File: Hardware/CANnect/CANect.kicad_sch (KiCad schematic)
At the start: 15 parts, among them J1 USB_C_Receptacle_USB2.0_16P, J2 Micro_SD_Card, J3 Conn_01x02_Pin, U1 SN65HVD230, U2 ESP32-S3-WROOM-1, U3 USBLC6-2SC6, U4 AP2114H-3.3TRG1

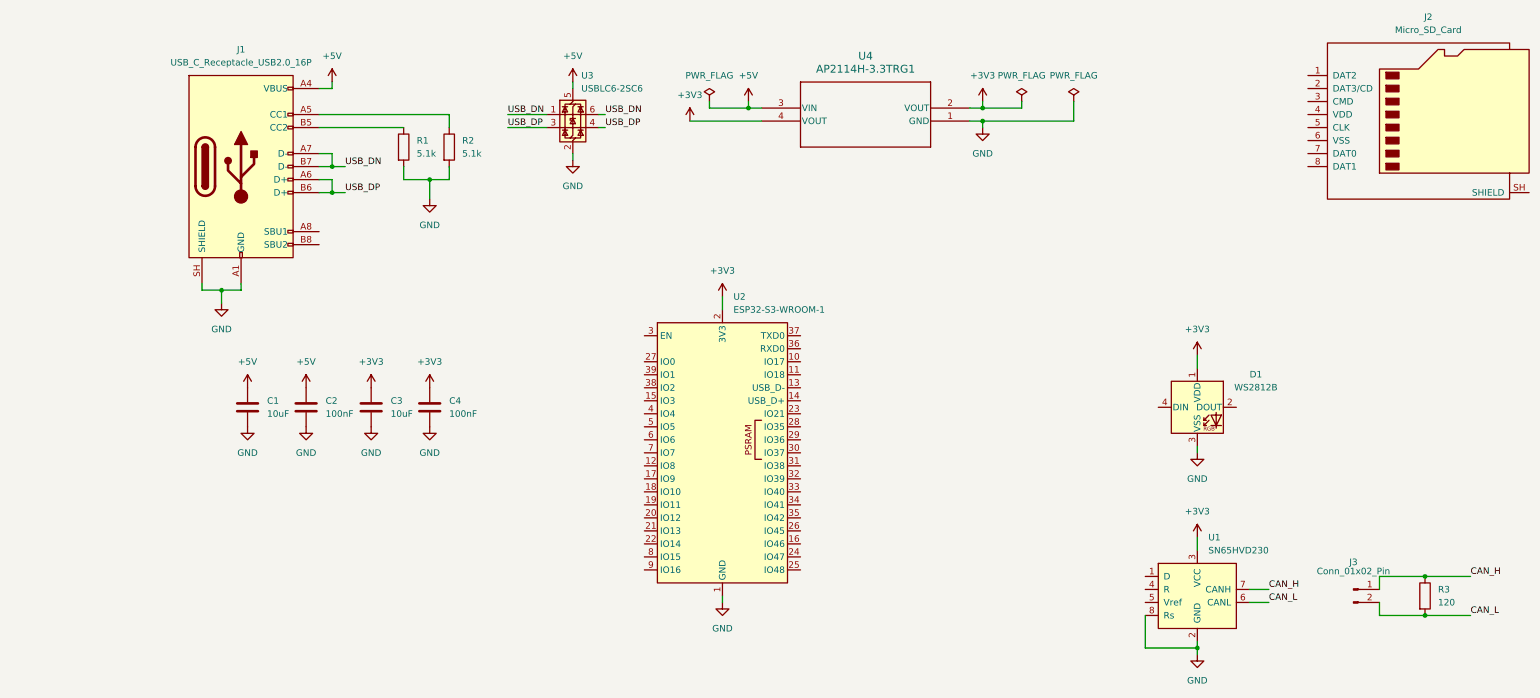
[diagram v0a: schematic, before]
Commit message: chore: initial monorepo structure with completed V0 USB-CAN hardware routing
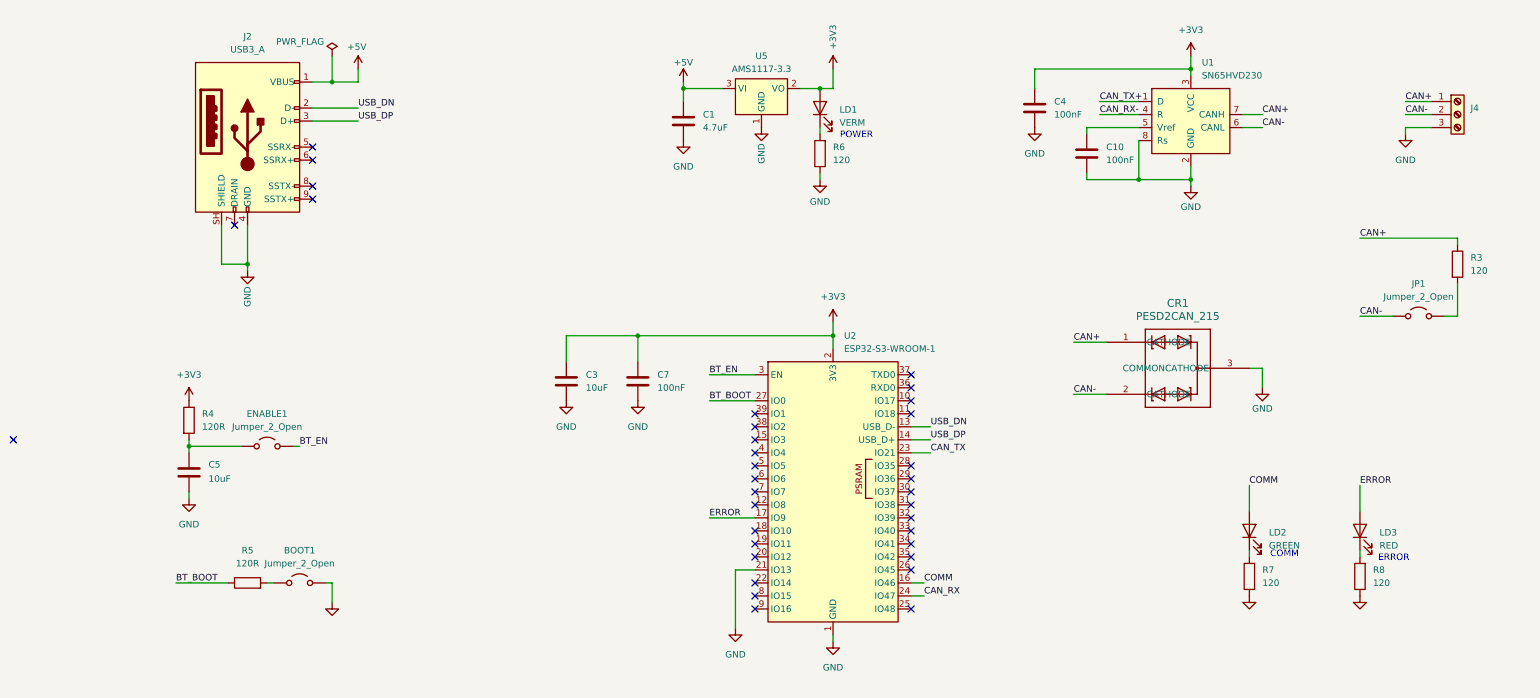
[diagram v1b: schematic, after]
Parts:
- removed C2: 100nF, Capacitor_SMD:C_0603_1608Metric, symbol Device:C
- removed D1: WS2812B, LED_SMD:LED_WS2812B_PLCC4_5.0x5.0mm_P3.2mm, symbol LED:WS2812B
- removed J1: USB_C_Receptacle_USB2.0_16P, Connector_USB:USB_C_Receptacle_HRO_TYPE-C-31-M-12, symbol Connector:USB_C_Receptacle_USB2.0_16P
- removed J2: Micro_SD_Card, Connector_Card:microSD_HC_Hirose_DM3D-SF, symbol Connector:Micro_SD_Card
- removed J3: Conn_01x02_Pin, symbol Connector:Conn_01x02_Pin
- removed R1, R2: 5.1k, Resistor_SMD:R_0805_2012Metric, symbol Device:R
- removed U3: USBLC6-2SC6, Package_TO_SOT_SMD:SOT-23-6, symbol Power_Protection:USBLC6-2SC6
- removed U4: AP2114H-3.3TRG1, Package_TO_SOT_SMD:SOT-223, symbol 2026-04-28_02-03-47:AP2114H-3.3TRG1
- added BOOT1, ENABLE1, JP1: Jumper_2_Open, Jumper:SolderJumper-2_P1.3mm_Open_RoundedPad1.0x1.5mm, symbol Jumper:Jumper_2_Open
- added C10, C7: 100nF, Capacitor_SMD:C_0402_1005Metric, symbol Device:C
- added C5: 10uF, Capacitor_SMD:C_0402_1005Metric, symbol Device:C
- added CR1: PESD2CAN_215, PCM_SparkFun-Semiconductor-Standard:SOT23-3, symbol PESD2CAN:PESD2CAN_215
- added J2: USB3_A, Connector_USB:USB3_A_Receptacle_Wuerth_692122030100, symbol Connector:USB3_A
- added J4: Screw_Terminal_01x03, TerminalBlock:TerminalBlock_MaiXu_MX126-5.0-03P_1x03_P5.00mm, symbol Connector:Screw_Terminal_01x03
- added LD1: VERM, LED_SMD:LED_0805_2012Metric, symbol Device:LED
- added LD2: GREEN, LED_SMD:LED_0805_2012Metric, symbol Device:LED
- added LD3: RED, LED_SMD:LED_0805_2012Metric, symbol Device:LED
- added R4, R5: 120R, PCM_SparkFun-Resistor:R_0402_1005Metric, symbol Device:R
- added R6: 120, Resistor_SMD:R_0805_2012Metric_Pad1.20x1.40mm_HandSolder, symbol Device:R
- added R7, R8: 120, PCM_SparkFun-Resistor:R_0402_1005Metric, symbol Device:R
- added U5: AMS1117-3.3, Package_TO_SOT_SMD:SOT-223-3_TabPin2, symbol Regulator_Linear:AMS1117-3.3
- C1: value 10uF -> 4.7uF; footprint Capacitor_SMD:C_0603_1608Metric -> Capacitor_SMD:C_0402_1005Metric
- C3, C4: footprint Capacitor_SMD:C_0603_1608Metric -> Capacitor_SMD:C_0402_1005Metric
- R3: footprint Resistor_SMD:R_0805_2012Metric -> PCM_SparkFun-Resistor:R_0402_1005Metric
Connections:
- net +3V3: now also C7.1, LD1.2 (A), R4.1, U5.2 (VO)
- net +5V: now also J2.1 (VBUS), U5.3 (VI)
- net GND: now also U2.21 (IO13), BOOT1.2 (B), C10.2, C5.2, C7.2, CR1.3 (COMMONCATHODE), J2.4 (GND), J2.SH (SHIELD), J4.3 (Pin_3), R6.1, R7.1, R8.1, U5.1 (GND)
- net USB_DN: now also U2.13 (USB_D-), J2.2 (D-)
- net USB_DP: now also U2.14 (USB_D+), J2.3 (D+)
- net COMM: now reaches U2.16 (IO46)
- net COMM: now also LD2.2 (A)
- net ERROR: now reaches U2.17 (IO9)
- net ERROR: now also LD3.2 (A)
- net CAN_TX: now reaches U2.23 (IO21)
- net CAN_RX: now reaches U2.24 (IO47)
- net BT_BOOT: now reaches U2.27 (IO0)
- net BT_BOOT: now also R5.1
- net BT_EN: now reaches U2.3 (EN)
- net BT_EN: now also ENABLE1.2 (B)
- net CAN_TX+: now reaches U1.1 (D)
- net CAN_RX-: now reaches U1.4 (R)
- net at U1.5 (Vref): now also C10.1
- net CAN_H renamed CAN+
- net CAN+: now also CR1.1 (CATHODE), J4.1 (Pin_1)
- net CAN_L: no longer names the net of R3.2
- net CAN_L: now also JP1.2 (B); no longer U1.6 (CANL)
- new net: C5.1, ENABLE1.1 (A), R4.2
- new net: LD2.1 (K), R7.2
- new net: LD1.1 (K), R6.2
- new net: LD3.1 (K), R8.2
- new net: BOOT1.1 (A), R5.2
- new net CAN-: CR1.2 (CATHODE), J4.2 (Pin_2), JP1.1 (A), U1.6 (CANL)
- no-connect marks 0 -> 34
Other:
- note added: "COMM"
- note added: "ERROR"
- note added: "POWER"
- moved on the sheet: C1, C3, C4, R3, U1, U2
